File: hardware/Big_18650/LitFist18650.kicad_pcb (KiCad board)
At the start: 2 copper layers, 95.8 x 15.2 mm, 40 parts, among them J1 PWM, J2 USB_B_Micro, J3 Battery, J4 ISP, Q1 NTR4003NT1G, Q2 NTR4003NT1G, Q3 NTR4003NT1G, SW1 Mode, SW2 Power, U1 ATtiny85-20SU, U2 MCP73831T-2ACI/OT, U3 PAM2401-8MSOP

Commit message: misc save
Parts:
- J3: footprint Jeremy:Battery_Clips_8650 -> Jeremy:Battery_Clips_18650
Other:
- board text added: "Lit Fist rev2 Jeremy Gillick 2018"
- board text removed: "Blinky Fist rev2 Jeremy Gillick 2018"
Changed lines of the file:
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@@
     (35 F.Paste user)
     (36 B.SilkS user)
-    (37 F.SilkS user)
+    (37 F.SilkS user hide)
     (38 B.Mask user)
     (39 F.Mask user)
@@
   )
   (setup
-    (last_trace_width 0.154)
+    (last_trace_width 0.1524)
     (user_trace_width 0.154)
     (user_trace_width 0.254)
@@
     (add_net RST)
     (add_net Vin)
-  )
-  (module Jeremy:Battery_Clips_8650 (layer B.Cu)
-    (at 139.32 91.1 180)
-    (fp_text reference J3 (at 0 7.0104 180) (layer B.SilkS) hide
-      (effects (font (size 1 1) (thickness 0.15)) (justify mirror))
-    )
-    (fp_text value Battery (at 0 -6.7056 180) (layer B.Fab) hide
-      (effects (font (size 1 1) (thickness 0.15)) (justify mirror))
-    )
-    (fp_line (start -22.22 5.6) (end -22.22 -5.6) (layer B.CrtYd) (width 0.15))
-    (fp_text user - (at -10 0.2032 180) (layer B.SilkS)
-      (effects (font (size 2.5 2.5) (thickness 0.15)) (justify mirror))
-    )
-    (fp_text user + (at 11 0.2032 180) (layer B.SilkS)
-      (effects (font (size 2.5 2.5) (thickness 0.15)) (justify mirror))
-    )
-    (fp_line (start -8 -2) (end -8 2) (layer B.SilkS) (width 0.3))
-    (fp_line (start 8 -2) (end -8 -2) (layer B.SilkS) (width 0.3))
-    (fp_line (start 8 -1) (end 8 -2) (layer B.SilkS) (width 0.3))
-    (fp_line (start 9 -1) (end 8 -1) (layer B.SilkS) (width 0.3))
-    (fp_line (start 9 0.9) (end 9 -1) (layer B.SilkS) (width 0.3))
-    (fp_line (start 8.1 0.9) (end 9 0.9) (layer B.SilkS) (width 0.3))
-    (fp_line (start 8.1 2) (end 8.1 0.9) (layer B.SilkS) (width 0.3))
-    (fp_line (start -8 2) (end 8.1 2) (layer B.SilkS) (width 0.3))
-    (fp_line (start -35.22 5.6) (end -22.22 5.6) (layer B.CrtYd) (width 0.15))
-    (fp_line (start -35.22 -5.6) (end -35.22 5.6) (layer B.CrtYd) (width 0.15))
-    (fp_line (start -22.22 -5.6) (end -35.22 -5.6) (layer B.CrtYd) (width 0.15))
-    (fp_line (start 35.22 5.6) (end 35.22 -5.6) (layer B.CrtYd) (width 0.15))
-    (fp_line (start 22.22 5.6) (end 22.22 -5.6) (layer B.CrtYd) (width 0.15))
-    (fp_line (start 35.22 5.6) (end 22.22 5.6) (layer B.CrtYd) (width 0.15))
-    (fp_line (start 22.22 -5.6) (end 35.22 -5.6) (layer B.CrtYd) (width 0.15))
-    (pad 2 thru_hole circle (at -24 2.54 180) (size 2.8 2.8) (drill 1.83) (layers *.Cu *.Mask)
-      (net 1 GND))
-    (pad 2 thru_hole circle (at -24 -2.54 180) (size 2.8 2.8) (drill 1.83) (layers *.Cu *.Mask)
-      (net 1 GND))
-    (pad 1 thru_hole circle (at 24 2.54 180) (size 2.8 2.8) (drill 1.83) (layers *.Cu *.Mask)
-      (net 22 +BATT))
-    (pad 1 thru_hole circle (at 24 -2.54 180) (size 2.8 2.8) (drill 1.83) (layers *.Cu *.Mask)
-      (net 22 +BATT))
-    (pad 1 thru_hole circle (at 31.62 0 180) (size 2.8 2.8) (drill 1.83) (layers *.Cu *.Mask)
-      (net 22 +BATT))
-    (pad 2 thru_hole circle (at -31.62 0 180) (size 2.8 2.8) (drill 1.83) (layers *.Cu *.Mask)
-      (net 1 GND))
   )
   (module Jeremy:Switch_SPST_GPTS203211BR2 (layer F.Cu)
@@
       (xy -2.549664 -1.91989) (xy -2.469928 -1.911165) (xy -2.400256 -1.919918)) (layer B.SilkS) (width 0.01))
   )
+  (module Jeremy:Battery_Clips_18650 (layer B.Cu)
+    (at 139.32 91.1 180)
+    (fp_text reference J3 (at 0 7.0104 180) (layer B.SilkS) hide
+      (effects (font (size 1 1) (thickness 0.15)) (justify mirror))
+    )
+    (fp_text value Battery (at 0 -6.7056 180) (layer B.Fab) hide
+      (effects (font (size 1 1) (thickness 0.15)) (justify mirror))
+    )
+    (fp_line (start -22.22 5.6) (end -22.22 -5.6) (layer B.CrtYd) (width 0.15))
+    (fp_text user - (at -10 0.2032 180) (layer B.SilkS)
+      (effects (font (size 2.5 2.5) (thickness 0.15)) (justify mirror))
+    )
+    (fp_text user + (at 11 0.2032 180) (layer B.SilkS)
+      (effects (font (size 2.5 2.5) (thickness 0.15)) (justify mirror))
+    )
+    (fp_line (start -8 -2) (end -8 2) (layer B.SilkS) (width 0.3))
+    (fp_line (start 8 -2) (end -8 -2) (layer B.SilkS) (width 0.3))
+    (fp_line (start 8 -1) (end 8 -2) (layer B.SilkS) (width 0.3))
+    (fp_line (start 9 -1) (end 8 -1) (layer B.SilkS) (width 0.3))
+    (fp_line (start 9 0.9) (end 9 -1) (layer B.SilkS) (width 0.3))
+    (fp_line (start 8.1 0.9) (end 9 0.9) (layer B.SilkS) (width 0.3))
+    (fp_line (start 8.1 2) (end 8.1 0.9) (layer B.SilkS) (width 0.3))
+    (fp_line (start -8 2) (end 8.1 2) (layer B.SilkS) (width 0.3))
+    (fp_line (start -35.22 5.6) (end -22.22 5.6) (layer B.CrtYd) (width 0.15))
+    (fp_line (start -35.22 -5.6) (end -35.22 5.6) (layer B.CrtYd) (width 0.15))
+    (fp_line (start -22.22 -5.6) (end -35.22 -5.6) (layer B.CrtYd) (width 0.15))
+    (fp_line (start 35.22 5.6) (end 35.22 -5.6) (layer B.CrtYd) (width 0.15))
+    (fp_line (start 22.22 5.6) (end 22.22 -5.6) (layer B.CrtYd) (width 0.15))
+    (fp_line (start 35.22 5.6) (end 22.22 5.6) (layer B.CrtYd) (width 0.15))
+    (fp_line (start 22.22 -5.6) (end 35.22 -5.6) (layer B.CrtYd) (width 0.15))
+    (fp_text user 18650 (at 0 0 180) (layer B.SilkS)
+      (effects (font (size 1 1) (thickness 0.15)) (justify mirror))
+    )
+    (pad 2 thru_hole circle (at -24 2.54 180) (size 2.8 2.8) (drill 1.83) (layers *.Cu *.Mask)
+      (net 1 GND))
+    (pad 2 thru_hole circle (at -24 -2.54 180) (size 2.8 2.8) (drill 1.83) (layers *.Cu *.Mask)
+      (net 1 GND))
+    (pad 1 thru_hole circle (at 24 2.54 180) (size 2.8 2.8) (drill 1.83) (layers *.Cu *.Mask)
+      (net 22 +BATT))
+    (pad 1 thru_hole circle (at 24 -2.54 180) (size 2.8 2.8) (drill 1.83) (layers *.Cu *.Mask)
+      (net 22 +BATT))
+    (pad 1 thru_hole circle (at 31.62 0 180) (size 2.8 2.8) (drill 1.83) (layers *.Cu *.Mask)
+      (net 22 +BATT))
+    (pad 2 thru_hole circle (at -31.62 0 180) (size 2.8 2.8) (drill 1.83) (layers *.Cu *.Mask)
+      (net 1 GND))
+  )
   (gr_text PWM (at 158.575 86.15) (layer B.SilkS)
     (effects (font (size 1.5 1.5) (thickness 0.2)) (justify mirror))
@@
   (gr_arc (start 98.5 97.7) (end 97.5 97.7) (angle -90) (layer Edge.Cuts) (width 0.15))
   (gr_arc (start 98.5 84.5) (end 97.5 84.5) (angle 90) (layer Edge.Cuts) (width 0.15))
-  (gr_text "Blinky Fist rev2\nJeremy Gillick\n2018" (at 184.8 87.95) (layer B.SilkS)
+  (gr_text "Lit Fist rev2\nJeremy Gillick\n2018" (at 184.8 87.95) (layer B.SilkS)
     (effects (font (size 1.2 1.2) (thickness 0.15)) (justify mirror))
   )
@@
   (gr_line (start 98.5 98.7) (end 192.35 98.7) (layer Edge.Cuts) (width 0.15))
   (gr_line (start 97.5 84.5) (end 97.5 97.7) (layer Edge.Cuts) (width 0.15))
-  (segment (start 143.95 89.775) (end 143.95 89.425) (width 0.254) (layer F.Cu) (net 7) (status 30))
-  (segment (start 149.1 89.725) (end 149.1 89.675) (width 0.254) (layer F.Cu) (net 7) (status 30))
-  (via (at 155 89.05) (size 0.6858) (drill 0.3302) (layers F.Cu B.Cu) (net 7))
-  (segment (start 154.325 89.725) (end 155 89.05) (width 0.254) (layer F.Cu) (net 7) (status 10))
-  (segment (start 154.3 89.725) (end 154.325 89.725) (width 0.254) (layer F.Cu) (net 7) (status 30))
-  (via (at 149.8 89) (size 0.6858) (drill 0.3302) (layers F.Cu B.Cu) (net 7))
-  (segment (start 149.1 89.7) (end 149.8 89) (width 0.254) (layer F.Cu) (net 7) (status 10))
-  (segment (start 149.1 89.725) (end 149.1 89.7) (width 0.254) (layer F.Cu) (net 7) (status 30))
-  (via (at 144.675 89.05) (size 0.6858) (drill 0.3302) (layers F.Cu B.Cu) (net 7))
-  (segment (start 143.95 89.775) (end 144.675 89.05) (width 0.254) (layer F.Cu) (net 7) (status 10))
   (segment (start 99.515 88.615) (end 99.785 88.345) (width 0.254) (layer F.Cu) (net 1) (status 30))
   (segment (start 99.515 90.115) (end 99.515 88.615) (width 0.254) (layer F.Cu) (net 1) (status 30))
@@
   (segment (start 167.025 95.7) (end 191.6 95.7) (width 0.154) (layer F.Cu) (net 5) (status 20))
   (segment (start 170.25 97.55) (end 172.0625 97.55) (width 0.254) (layer F.Cu) (net 6) (status 30))
+  (segment (start 143.95 89.775) (end 143.95 89.425) (width 0.254) (layer F.Cu) (net 7) (status 30))
+  (segment (start 149.1 89.725) (end 149.1 89.675) (width 0.254) (layer F.Cu) (net 7) (status 30))
+  (via (at 155 89.05) (size 0.6858) (drill 0.3302) (layers F.Cu B.Cu) (net 7))
+  (segment (start 154.325 89.725) (end 155 89.05) (width 0.254) (layer F.Cu) (net 7) (status 10))
+  (segment (start 154.3 89.725) (end 154.325 89.725) (width 0.254) (layer F.Cu) (net 7) (status 30))
+  (via (at 149.8 89) (size 0.6858) (drill 0.3302) (layers F.Cu B.Cu) (net 7))
+  (segment (start 149.1 89.7) (end 149.8 89) (width 0.254) (layer F.Cu) (net 7) (status 10))
+  (segment (start 149.1 89.725) (end 149.1 89.7) (width 0.254) (layer F.Cu) (net 7) (status 30))
+  (via (at 144.675 89.05) (size 0.6858) (drill 0.3302) (layers F.Cu B.Cu) (net 7))
+  (segment (start 143.95 89.775) (end 144.675 89.05) (width 0.254) (layer F.Cu) (net 7) (status 10))
   (via (at 191.6 84.925) (size 0.6858) (drill 0.3302) (layers F.Cu B.Cu) (net 7))
   (segment (start 191.6 86.5) (end 191.6 84.925) (width 0.254) (layer F.Cu) (net 7) (status 10))

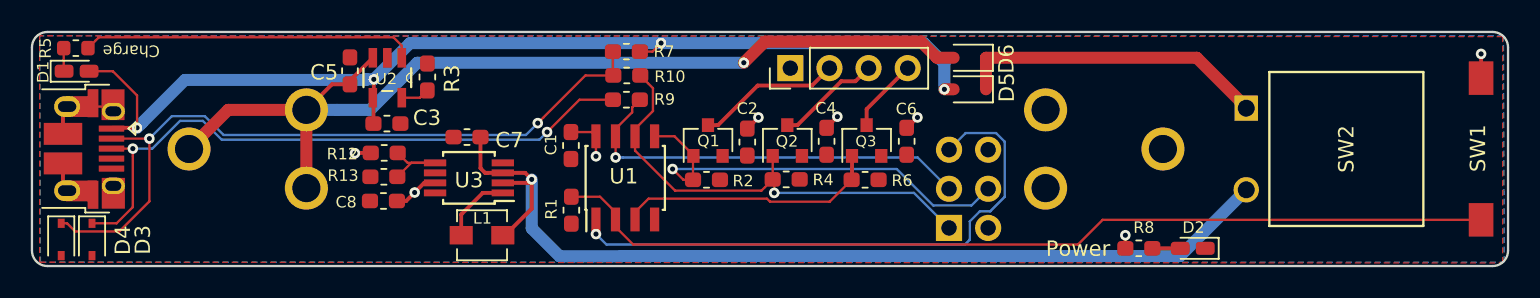
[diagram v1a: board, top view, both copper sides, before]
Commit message: Fix Attiny footprint. Add debounce circuit.
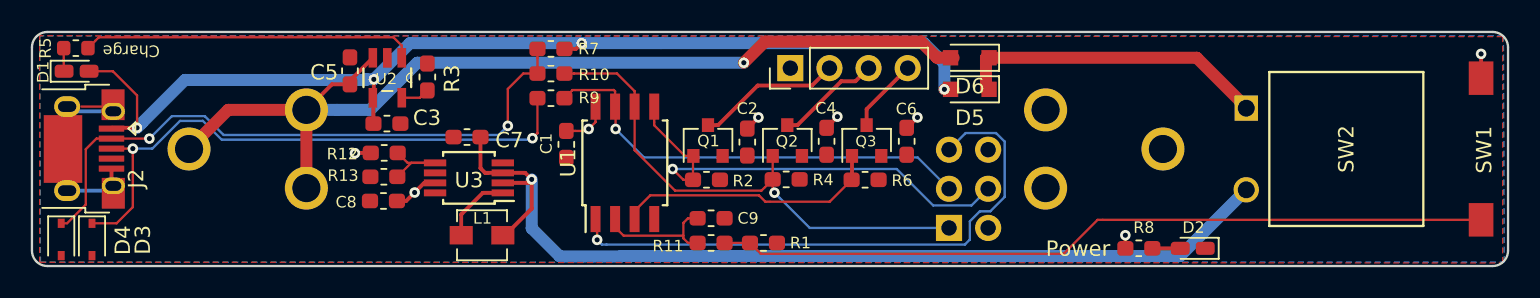
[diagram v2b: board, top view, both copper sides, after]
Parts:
- added C9: 0.1uF, Capacitor_SMD:C_0603_1608Metric_Pad1.05x0.95mm_HandSolder, F.Cu at (141.6, 95.6)
- added R11: 330, Resistor_SMD:R_0603_1608Metric_Pad1.05x0.95mm_HandSolder, F.Cu at (141.6, 97.2)
- D5, D6: footprint Diode_SMD:D_SOD-323 -> Diode_SMD:D_SOD-323_HandSoldering
- J2: footprint Connector_USB:USB_Micro-B_Amphenol_10103594-0001LF_Horizontal -> Jeremy:USB_Micro-B_Amphenol_10103594-0001LF_Horizontal
- U1: footprint Package_SO:SOIC-8_3.9x4.9mm_P1.27mm -> Package_SO:SOIJ-8_5.3x5.3mm_P1.27mm
- moved R1 12.7 mm to (145.0, 97.2), turned to 0 degrees
- moved R10 4.93 mm to (131.2, 86.2)
- moved R7 4.90 mm to (131.2, 84.6)
- moved R9 4.90 mm to (131.2, 87.8)
- moved U1 0.98 mm to (136.0, 92.0)
- moved C1 0.31 mm to (132.2, 90.8)
- turned SW1 to 90 degrees
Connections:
- SW1 pad 1: +5V -> Net-(R1-Pad1)
- SW1 pad 2: Net-(R1-Pad1) -> +5V
- U1 pad 2: Net-(R1-Pad1) -> Net-(C9-Pad1)
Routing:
- net Net-(R1-Pad1): track 61.6 -> 50.3 mm
- net Net-(C9-Pad1): track 0.00 -> 9.23 mm
- net GND: track 5.86 -> 13.3 mm
- net Net-(D4-Pad1): track 47.7 -> 41.1 mm
- net Net-(D3-Pad1): track 41.8 -> 38.2 mm
- net D-: track 30.8 -> 33.9 mm
- net D+: track 26.9 -> 29.3 mm
- net MOSI: track 28.2 -> 29.7 mm
